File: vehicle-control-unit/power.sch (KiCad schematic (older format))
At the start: 13 parts, among them J13 Conn_01x02_Male, SW1 SW_SPST, U4 MIC29502WT

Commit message: Route PCB
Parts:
- J10: renamed from J13; value Conn_01x02_Male -> Connector:Screw_Terminal_01x02; symbol Connector:Conn_01x02_Male -> Connector:Screw_Terminal_01x02
- U4: footprint Package_TO_SOT_THT:TO-220-5_P3.4x3.7mm_StaggerEven_Lead3.8mm_Vertical -> Package_TO_SOT_THT:TO-220-5_P3.4x3.8mm_StaggerEven_Lead7.13mm_TabDown
- renumbered C6 to C5, C7 to C6, C8 to C7
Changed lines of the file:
@@
 Sheet 3 3
 Title "Earth Rover"
-Date "2020-04-25"
-Rev "6"
+Date "2020-06-07"
+Rev "7"
 Comp "Vijfendertig BVBA"
 Comment1 "Maarten De Munck"
@@
 $EndComp
 $Comp
-L Device:C C8
+L Device:C C7
 U 1 1 5E015FEC
 P 3950 9250
-F 0 "C8" H 4065 9296 50  0000 L CNN
+F 0 "C7" H 4065 9296 50  0000 L CNN
 F 1 "100n" H 4065 9205 50  0000 L CNN
 F 2 "Capacitor_THT:C_Disc_D5.0mm_W2.5mm_P5.00mm" H 3988 9100 50  0001 C CNN
@@
 Connection ~ 3350 9050
 $Comp
-L power:GND #PWR045
+L power:GND #PWR042
 U 1 1 5E01F8D8
 P 3350 9500
-F 0 "#PWR045" H 3350 9250 50  0001 C CNN
+F 0 "#PWR042" H 3350 9250 50  0001 C CNN
 F 1 "GND" H 3355 9327 50  0000 C CNN
 F 2 "" H 3350 9500 50  0001 C CNN
@@
 $EndComp
 $Comp
-L power:GND #PWR040
+L power:GND #PWR037
 U 1 1 5E4FCEBE
 P 2550 8150
-F 0 "#PWR040" H 2550 7900 50  0001 C CNN
+F 0 "#PWR037" H 2550 7900 50  0001 C CNN
 F 1 "GND" H 2555 7977 50  0000 C CNN
 F 2 "" H 2550 8150 50  0001 C CNN
@@
 $EndComp
 $Comp
-L Connector:Conn_01x02_Male J13
+L Connector:Screw_Terminal_01x02 J10
 U 1 1 5E4FCACC
 P 2150 7550
-F 0 "J13" H 2258 7639 50  0000 C CNN
-F 1 "Conn_01x02_Male" H 2258 7640 50  0001 C CNN
+F 0 "J10" H 2150 7700 50  0000 C CNN
+F 1 "Connector:Screw_Terminal_01x02" H 2258 7640 50  0001 C CNN
 F 2 "TerminalBlock:TerminalBlock_bornier-2_P5.08mm" H 2150 7550 50  0001 C CNN
 F 3 "~" H 2150 7550 50  0001 C CNN
 	1    2150 7550
-	1    0    0    -1
-$EndComp
-$Comp
-L power:+BATT #PWR037
+	-1   0    0    -1
+$EndComp
+$Comp
+L power:+BATT #PWR034
 U 1 1 5E4FC127
 P 2550 7000
-F 0 "#PWR037" H 2550 6850 50  0001 C CNN
+F 0 "#PWR034" H 2550 6850 50  0001 C CNN
 F 1 "+BATT" H 2565 7173 50  0000 C CNN
 F 2 "" H 2550 7000 50  0001 C CNN
@@
 $EndComp
 $Comp
-L Device:CP C6
+L Device:CP C5
 U 1 1 5E4FBB47
 P 2950 7600
-F 0 "C6" H 3068 7646 50  0000 L CNN
+F 0 "C5" H 3068 7646 50  0000 L CNN
 F 1 "10u" H 3068 7555 50  0000 L CNN
 F 2 "Capacitor_THT:CP_Radial_D5.0mm_P2.50mm" H 2988 7450 50  0001 C CNN
@@
 $EndComp
 $Comp
-L power:GND #PWR041
+L power:GND #PWR038
 U 1 1 5E4FB89E
 P 2950 8150
-F 0 "#PWR041" H 2950 7900 50  0001 C CNN
+F 0 "#PWR038" H 2950 7900 50  0001 C CNN
 F 1 "GND" H 2955 7977 50  0000 C CNN
 F 2 "" H 2950 8150 50  0001 C CNN
@@
 	6050 8150 6050 7750
 $Comp
-L power:GND #PWR044
+L power:GND #PWR041
 U 1 1 5E50947F
 P 6050 8150
-F 0 "#PWR044" H 6050 7900 50  0001 C CNN
+F 0 "#PWR041" H 6050 7900 50  0001 C CNN
 F 1 "GND" H 6055 7977 50  0000 C CNN
 F 2 "" H 6050 8150 50  0001 C CNN
@@
 $EndComp
 $Comp
-L power:+5V #PWR038
+L power:+5V #PWR035
 U 1 1 5E4FD133
 P 6450 7000
-F 0 "#PWR038" H 6450 6850 50  0001 C CNN
+F 0 "#PWR035" H 6450 6850 50  0001 C CNN
 F 1 "+5V" H 6465 7173 50  0000 C CNN
 F 2 "" H 6450 7000 50  0001 C CNN
@@
 $EndComp
 $Comp
-L Device:CP C7
+L Device:CP C6
 U 1 1 5E4FBE0F
 P 6050 7600
-F 0 "C7" H 6168 7646 50  0000 L CNN
+F 0 "C6" H 6168 7646 50  0000 L CNN
 F 1 "22u" H 6168 7555 50  0000 L CNN
 F 2 "Capacitor_THT:CP_Radial_D5.0mm_P2.50mm" H 6088 7450 50  0001 C CNN
@@
 $EndComp
 $Comp
-L power:GND #PWR042
+L power:GND #PWR039
 U 1 1 5E4FB653
 P 4900 8150
-F 0 "#PWR042" H 4900 7900 50  0001 C CNN
+F 0 "#PWR039" H 4900 7900 50  0001 C CNN
 F 1 "GND" H 4905 7977 50  0000 C CNN
 F 2 "" H 4900 8150 50  0001 C CNN
@@
 $EndComp
 $Comp
-L power:GND #PWR043
+L power:GND #PWR040
 U 1 1 5E4FB449
 P 5650 8150
-F 0 "#PWR043" H 5650 7900 50  0001 C CNN
+F 0 "#PWR040" H 5650 7900 50  0001 C CNN
 F 1 "GND" H 5655 7977 50  0000 C CNN
 F 2 "" H 5650 8150 50  0001 C CNN
@@
 F 0 "U4" H 4900 7567 50  0000 C CNN
 F 1 "MIC29502WT" H 4900 7476 50  0000 C CNN
-F 2 "Package_TO_SOT_THT:TO-220-5_P3.4x3.7mm_StaggerEven_Lead3.8mm_Vertical" H 5000 6950 50  0001 L CNN
+F 2 "Package_TO_SOT_THT:TO-220-5_P3.4x3.8mm_StaggerEven_Lead7.13mm_TabDown" H 5000 6950 50  0001 L CNN
 F 3 "http://ww1.microchip.com/downloads/en/devicedoc/20005685a.pdf" H 4900 7200 50  0001 C CNN
 	1    4900 7200
@@
 $EndComp
 $Comp
-L power:GND #PWR039
+L power:GND #PWR036
 U 1 1 5E34A716
 P 4400 7850
-F 0 "#PWR039" H 4400 7600 50  0001 C CNN
+F 0 "#PWR036" H 4400 7600 50  0001 C CNN
 F 1 "GND" H 4405 7677 50  0000 C CNN
 F 2 "" H 4400 7850 50  0001 C CNN

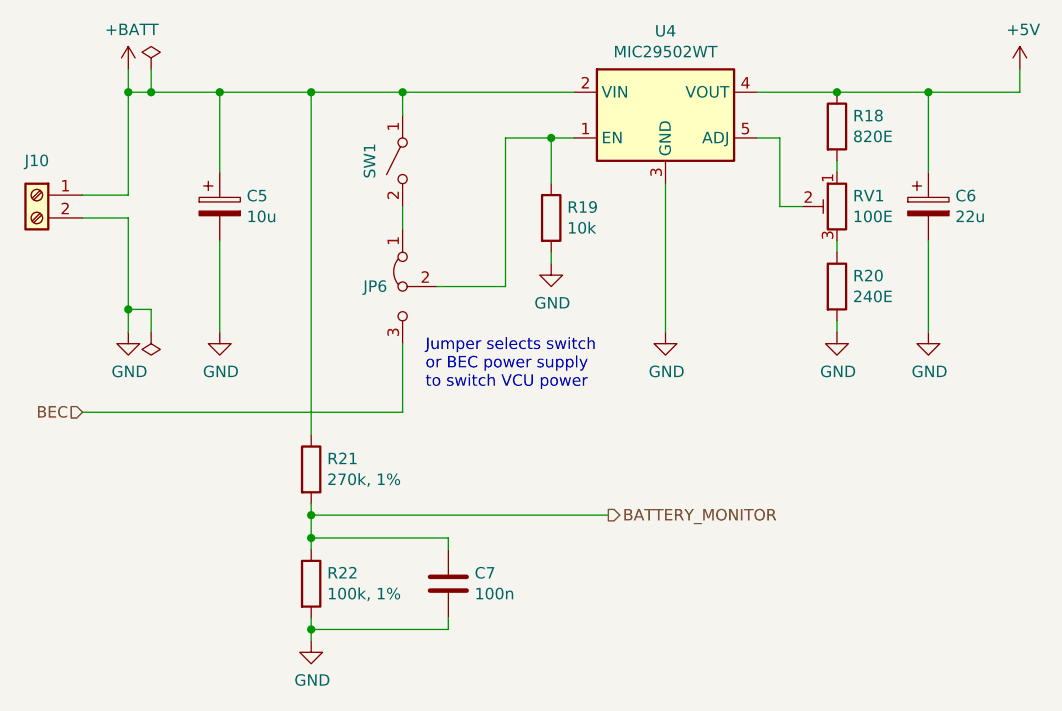
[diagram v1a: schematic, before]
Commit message: Clean up routing
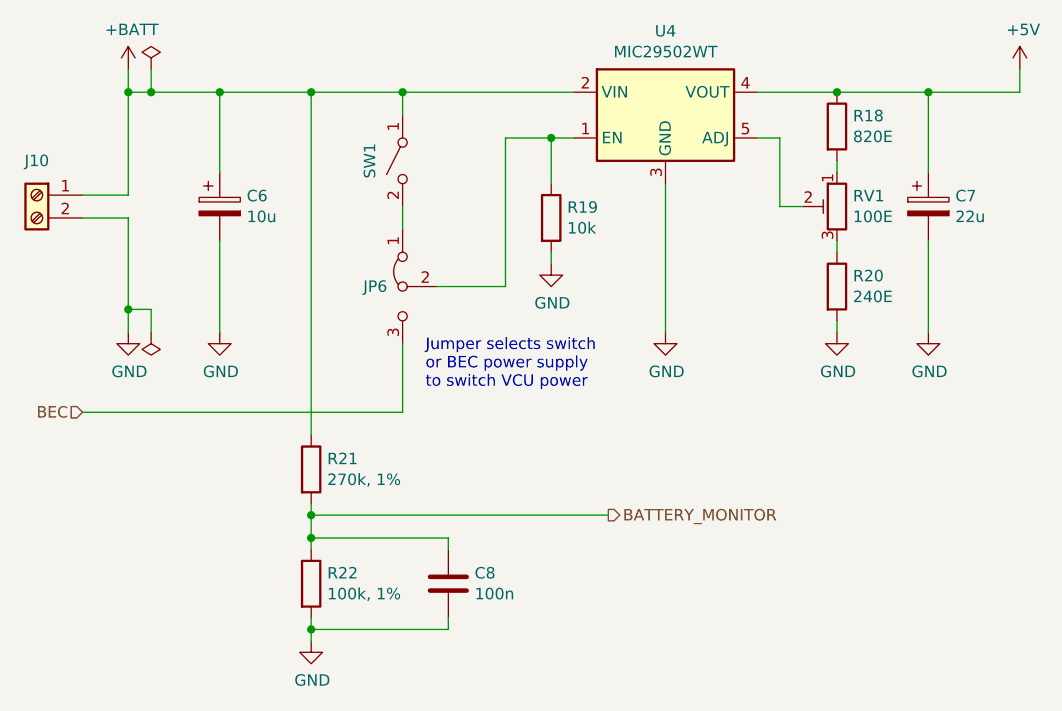
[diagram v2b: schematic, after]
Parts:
- renumbered C5 to C6, C6 to C7, C7 to C8
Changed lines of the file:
@@
 $EndComp
 $Comp
-L Device:C C7
+L Device:C C8
 U 1 1 5E015FEC
 P 3950 9250
-F 0 "C7" H 4065 9296 50  0000 L CNN
+F 0 "C8" H 4065 9296 50  0000 L CNN
 F 1 "100n" H 4065 9205 50  0000 L CNN
 F 2 "Capacitor_THT:C_Disc_D5.0mm_W2.5mm_P5.00mm" H 3988 9100 50  0001 C CNN
@@
 Connection ~ 3350 9050
 $Comp
-L power:GND #PWR042
+L power:GND #PWR044
 U 1 1 5E01F8D8
 P 3350 9500
-F 0 "#PWR042" H 3350 9250 50  0001 C CNN
+F 0 "#PWR044" H 3350 9250 50  0001 C CNN
 F 1 "GND" H 3355 9327 50  0000 C CNN
 F 2 "" H 3350 9500 50  0001 C CNN
@@
 $EndComp
 $Comp
-L power:GND #PWR037
+L power:GND #PWR039
 U 1 1 5E4FCEBE
 P 2550 8150
-F 0 "#PWR037" H 2550 7900 50  0001 C CNN
+F 0 "#PWR039" H 2550 7900 50  0001 C CNN
 F 1 "GND" H 2555 7977 50  0000 C CNN
 F 2 "" H 2550 8150 50  0001 C CNN
@@
 $EndComp
 $Comp
-L power:+BATT #PWR034
+L power:+BATT #PWR036
 U 1 1 5E4FC127
 P 2550 7000
-F 0 "#PWR034" H 2550 6850 50  0001 C CNN
+F 0 "#PWR036" H 2550 6850 50  0001 C CNN
 F 1 "+BATT" H 2565 7173 50  0000 C CNN
 F 2 "" H 2550 7000 50  0001 C CNN
@@
 $EndComp
 $Comp
-L Device:CP C5
+L Device:CP C6
 U 1 1 5E4FBB47
 P 2950 7600
-F 0 "C5" H 3068 7646 50  0000 L CNN
+F 0 "C6" H 3068 7646 50  0000 L CNN
 F 1 "10u" H 3068 7555 50  0000 L CNN
 F 2 "Capacitor_THT:CP_Radial_D5.0mm_P2.50mm" H 2988 7450 50  0001 C CNN
@@
 $EndComp
 $Comp
-L power:GND #PWR038
+L power:GND #PWR040
 U 1 1 5E4FB89E
 P 2950 8150
-F 0 "#PWR038" H 2950 7900 50  0001 C CNN
+F 0 "#PWR040" H 2950 7900 50  0001 C CNN
 F 1 "GND" H 2955 7977 50  0000 C CNN
 F 2 "" H 2950 8150 50  0001 C CNN
@@
 	6050 8150 6050 7750
 $Comp
-L power:GND #PWR041
+L power:GND #PWR043
 U 1 1 5E50947F
 P 6050 8150
-F 0 "#PWR041" H 6050 7900 50  0001 C CNN
+F 0 "#PWR043" H 6050 7900 50  0001 C CNN
 F 1 "GND" H 6055 7977 50  0000 C CNN
 F 2 "" H 6050 8150 50  0001 C CNN
@@
 $EndComp
 $Comp
-L power:+5V #PWR035
+L power:+5V #PWR037
 U 1 1 5E4FD133
 P 6450 7000
-F 0 "#PWR035" H 6450 6850 50  0001 C CNN
+F 0 "#PWR037" H 6450 6850 50  0001 C CNN
 F 1 "+5V" H 6465 7173 50  0000 C CNN
 F 2 "" H 6450 7000 50  0001 C CNN
@@
 $EndComp
 $Comp
-L Device:CP C6
+L Device:CP C7
 U 1 1 5E4FBE0F
 P 6050 7600
-F 0 "C6" H 6168 7646 50  0000 L CNN
+F 0 "C7" H 6168 7646 50  0000 L CNN
 F 1 "22u" H 6168 7555 50  0000 L CNN
 F 2 "Capacitor_THT:CP_Radial_D5.0mm_P2.50mm" H 6088 7450 50  0001 C CNN
@@
 $EndComp
 $Comp
-L power:GND #PWR039
+L power:GND #PWR041
 U 1 1 5E4FB653
 P 4900 8150
-F 0 "#PWR039" H 4900 7900 50  0001 C CNN
+F 0 "#PWR041" H 4900 7900 50  0001 C CNN
 F 1 "GND" H 4905 7977 50  0000 C CNN
 F 2 "" H 4900 8150 50  0001 C CNN
@@
 $EndComp
 $Comp
-L power:GND #PWR040
+L power:GND #PWR042
 U 1 1 5E4FB449
 P 5650 8150
-F 0 "#PWR040" H 5650 7900 50  0001 C CNN
+F 0 "#PWR042" H 5650 7900 50  0001 C CNN
 F 1 "GND" H 5655 7977 50  0000 C CNN
 F 2 "" H 5650 8150 50  0001 C CNN
@@
 $EndComp
 $Comp
-L power:GND #PWR036
+L power:GND #PWR038
 U 1 1 5E34A716
 P 4400 7850
-F 0 "#PWR036" H 4400 7600 50  0001 C CNN
+F 0 "#PWR038" H 4400 7600 50  0001 C CNN
 F 1 "GND" H 4405 7677 50  0000 C CNN
 F 2 "" H 4400 7850 50  0001 C CNN
